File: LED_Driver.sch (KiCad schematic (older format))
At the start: 6 parts

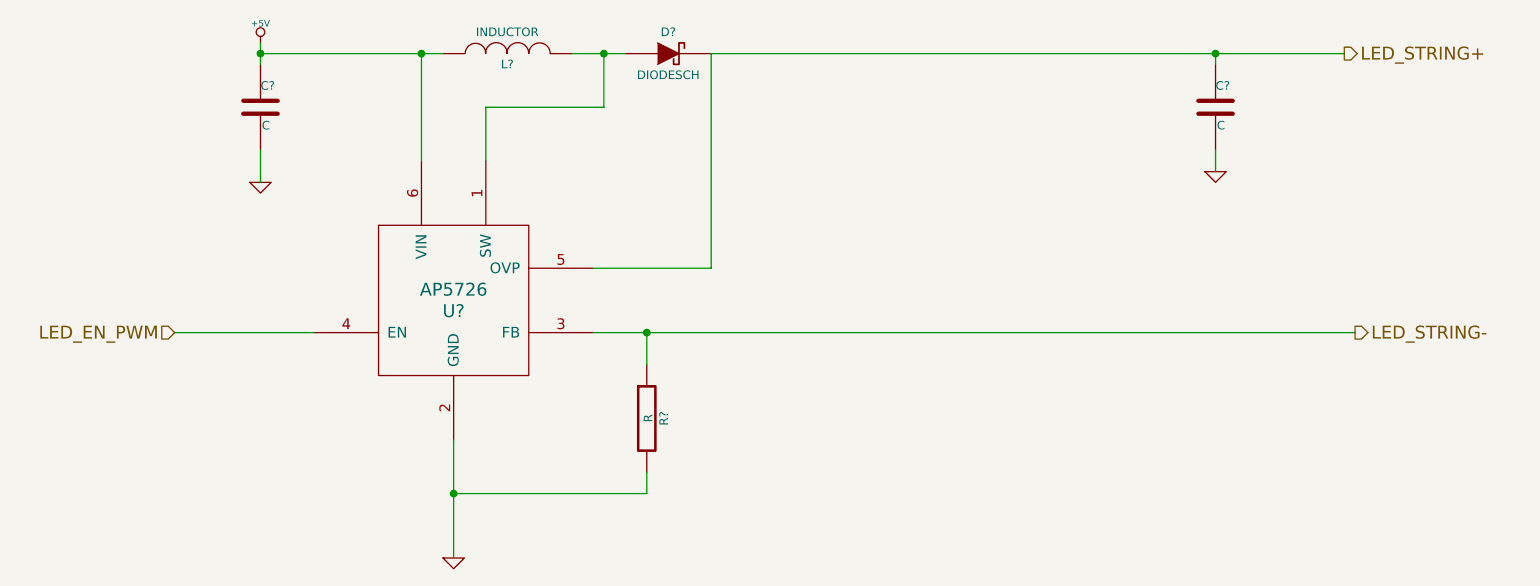
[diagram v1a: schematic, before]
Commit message: associating and placing relay module
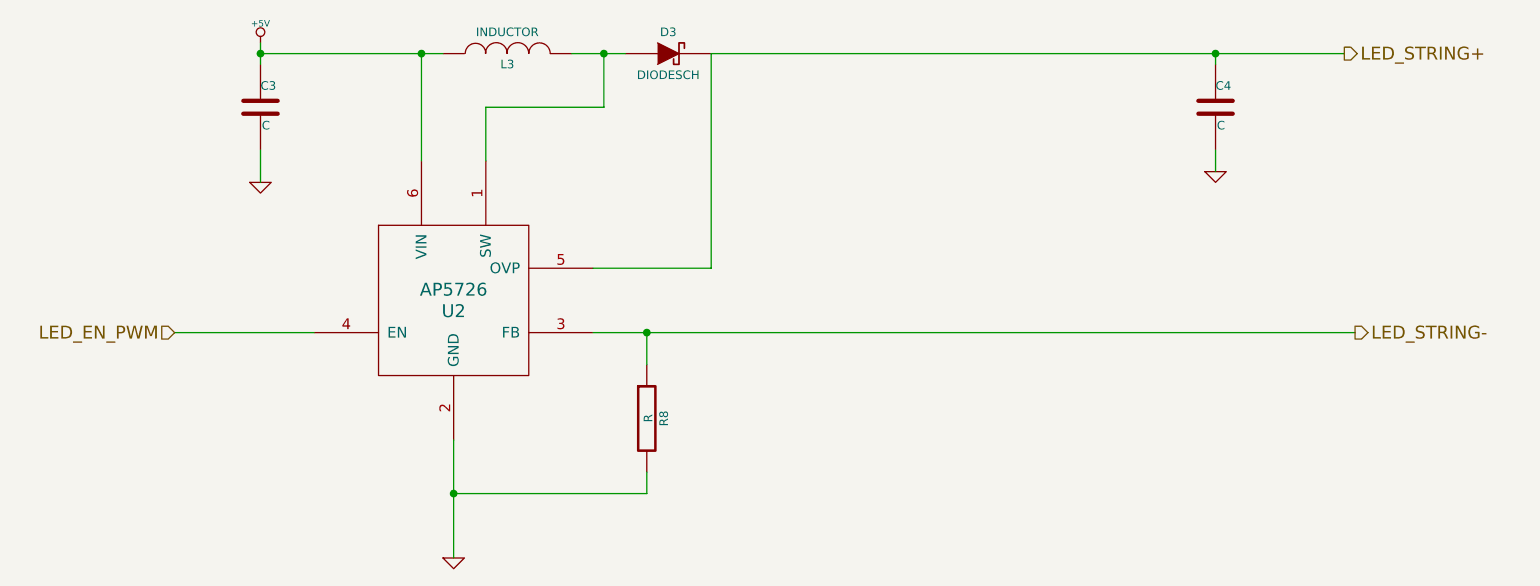
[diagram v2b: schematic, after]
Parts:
- gave numbers to parts that had none: 6
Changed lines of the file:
@@
 Sheet 5 9
 Title ""
-Date "10 feb 2014"
+Date "22 feb 2014"
 Rev ""
 Comp ""
@@
 LED_STRING-
 $Comp
-L AP5726 U?
+L AP5726 U2
 U 1 1 52F53D10
 P 4600 4250
-F 0 "U?" H 4600 4200 60  0000 C CNN
+F 0 "U2" H 4600 4200 60  0000 C CNN
 F 1 "AP5726" H 4600 4300 60  0000 C CNN
 F 2 "" H 4550 4250 60  0000 C CNN
@@
 $EndComp
 $Comp
-L +5V #PWR?
+L +5V #PWR016
 U 1 1 52F53D61
 P 3700 3050
-F 0 "#PWR?" H 3700 3140 20  0001 C CNN
+F 0 "#PWR016" H 3700 3140 20  0001 C CNN
 F 1 "+5V" H 3700 3140 30  0000 C CNN
 F 2 "" H 3700 3050 60  0000 C CNN
@@
 $EndComp
 $Comp
-L GND #PWR?
+L GND #PWR017
 U 1 1 52F53D70
 P 3700 3700
-F 0 "#PWR?" H 3700 3700 30  0001 C CNN
+F 0 "#PWR017" H 3700 3700 30  0001 C CNN
 F 1 "GND" H 3700 3630 30  0001 C CNN
 F 2 "" H 3700 3700 60  0000 C CNN
@@
 $EndComp
 $Comp
-L GND #PWR?
+L GND #PWR018
 U 1 1 52F53D87
 P 4600 5450
-F 0 "#PWR?" H 4600 5450 30  0001 C CNN
+F 0 "#PWR018" H 4600 5450 30  0001 C CNN
 F 1 "GND" H 4600 5380 30  0001 C CNN
 F 2 "" H 4600 5450 60  0000 C CNN
@@
 $EndComp
 $Comp
-L C C?
+L C C3
 U 1 1 52F53D91
 P 3700 3350
-F 0 "C?" H 3700 3450 40  0000 L CNN
+F 0 "C3" H 3700 3450 40  0000 L CNN
 F 1 "C" H 3706 3265 40  0000 L CNN
 F 2 "~" H 3738 3200 30  0000 C CNN
@@
 $EndComp
 $Comp
-L INDUCTOR L?
+L INDUCTOR L3
 U 1 1 52F53DB6
 P 4850 3100
-F 0 "L?" V 4800 3100 40  0000 C CNN
+F 0 "L3" V 4800 3100 40  0000 C CNN
 F 1 "INDUCTOR" V 4950 3100 40  0000 C CNN
 F 2 "~" H 4850 3100 60  0000 C CNN
@@
 $EndComp
 $Comp
-L DIODESCH D?
+L DIODESCH D3
 U 1 1 52F53DD8
 P 5600 3100
-F 0 "D?" H 5600 3200 40  0000 C CNN
+F 0 "D3" H 5600 3200 40  0000 C CNN
 F 1 "DIODESCH" H 5600 3000 40  0000 C CNN
 F 2 "~" H 5600 3100 60  0000 C CNN
@@
 	3950 4400 3300 4400
 Wire Wire Line
-	4600 4900 4600 5150
+	4600 4900 4600 5450
 Wire Wire Line
-	4600 5150 4600 5450
-Wire Wire Line
-	3700 3050 3700 3100
-Wire Wire Line
-	3700 3100 3700 3150
+	3700 3050 3700 3150
 Wire Wire Line
 	3700 3550 3700 3700
 Wire Wire Line
-	3700 3100 4450 3100
-Wire Wire Line
-	4450 3100 4550 3100
+	3700 3100 4550 3100
 Wire Wire Line
 	4450 3100 4450 3600
@@
 Connection ~ 4450 3100
 Wire Wire Line
-	5150 3100 5300 3100
-Wire Wire Line
-	5300 3100 5400 3100
+	5150 3100 5400 3100
 Wire Wire Line
 	5300 3100 5300 3350
@@
 	5800 4100 5250 4100
 $Comp
-L C C?
+L C C4
 U 1 1 52F53E10
 P 8150 3350
-F 0 "C?" H 8150 3450 40  0000 L CNN
+F 0 "C4" H 8150 3450 40  0000 L CNN
 F 1 "C" H 8156 3265 40  0000 L CNN
 F 2 "~" H 8188 3200 30  0000 C CNN
@@
 $EndComp
 Wire Wire Line
-	5800 3100 8150 3100
-Wire Wire Line
-	8150 3100 8750 3100
+	5800 3100 8750 3100
 Wire Wire Line
 	8150 3100 8150 3150
 Connection ~ 8150 3100
 $Comp
-L GND #PWR?
+L GND #PWR019
 U 1 1 52F53E41
 P 8150 3650
-F 0 "#PWR?" H 8150 3650 30  0001 C CNN
+F 0 "#PWR019" H 8150 3650 30  0001 C CNN
 F 1 "GND" H 8150 3580 30  0001 C CNN
 F 2 "" H 8150 3650 60  0000 C CNN
@@
 	8150 3550 8150 3650
 $Comp
-L R R?
+L R R8
 U 1 1 52F53E60
 P 5500 4800
-F 0 "R?" V 5580 4800 40  0000 C CNN
+F 0 "R8" V 5580 4800 40  0000 C CNN
 F 1 "R" V 5507 4801 40  0000 C CNN
 F 2 "~" V 5430 4800 30  0000 C CNN
@@
 $EndComp
 Wire Wire Line
-	5250 4400 5500 4400
-Wire Wire Line
-	5500 4400 8800 4400
+	5250 4400 8800 4400
 Wire Wire Line
 	5500 4400 5500 4550
